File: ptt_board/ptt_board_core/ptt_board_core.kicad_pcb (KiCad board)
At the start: 2 copper layers, 25 x 25 mm, 14 parts, among them P0.03 TestPoint, P0.07 TestPoint, P0.30 TestPoint, P26 Conn_01x01_Pin, U1 SKB369

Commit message: [WIP] Started net rev of ptt board and radio board
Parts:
- removed BT1: MY-1632-03-R, Project_components:BAT-SMD_MY-1632-03
- removed Batt+1, P.0.31, P0.03, P0.07, P0.30, Reset1: TestPoint, TestPoint:TestPoint_Pad_D1.0mm
- removed IO1, P26: Conn_01x01_Pin, Connector_PinHeader_2.54mm:PinHeader_1x01_P2.54mm_Vertical
- added Batt1: TestPoint, TestPoint:TestPoint_Pad_D1.0mm, F.Cu at (102.5, 110.8)
- added Batt2: Conn_01x01_Pin, Connector_Pin:Pin_D1.0mm_L10.0mm, F.Cu at (106.5, 109.5)
- added GND3: TestPoint, TestPoint:TestPoint_Pad_D1.0mm, F.Cu at (101.2, 110.8)
- added IO2: TestPoint, TestPoint:TestPoint_Pad_D1.0mm, F.Cu at (100.0, 110.8)
- added P0.26: TestPoint, TestPoint:TestPoint_Pad_D1.0mm, F.Cu at (97.4, 110.8)
- added P026: Conn_01x01_Pin, Connector_Pin:Pin_D1.0mm_L10.0mm, F.Cu at (88.8, 100.8)
- added R1: 470k, Resistor_SMD:R_0603_1608Metric_Pad0.98x0.95mm_HandSolder, F.Cu at (93.5, 105.9)
- added SW1: RKB2SJG250SMTRLFS, Project_components:Push button C2927788, F.Cu at (100.0, 100.0)
- C1, C2, U1: moved to B.Cu
- CLK1: value Conn_01x01_Pin -> TestPoint; footprint Connector_PinHeader_2.54mm:PinHeader_1x01_P2.54mm_Vertical -> TestPoint:TestPoint_Pad_D1.0mm
- Gnd1: footprint Connector_PinHeader_2.54mm:PinHeader_1x01_P2.54mm_Vertical -> Connector_Pin:Pin_D1.0mm_L10.0mm
- moved C1 20.3 mm to (110.5, 96.0), turned to 0 degrees
- moved C2 15.7 mm to (110.5, 98.0)
- moved CLK1 11.3 mm to (98.7, 110.8), turned to -90 degrees
- moved Gnd1 4.51 mm to (111.5, 100.8)
- moved U1 0.51 mm to (100.0, 98.2), turned to 180 degrees
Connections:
- U1 pad 12: Net-(U1-P0.03) -> unconnected-(U1-P0.03-Pad12)
- U1 pad 14: Net-(U1-P0.07) -> unconnected-(U1-P0.07-Pad14)
- U1 pad 22: Reset -> unconnected-(U1-P0.21/~{RESET}-Pad22)
- U1 pad 4: Net-(P26-Pin_1) -> P0.26
- U1 pad 6: unconnected-(U1-P0.28-Pad6) -> P0.28
- U1 pad 8: Net-(U1-P0.30) -> unconnected-(U1-P0.30-Pad8)
- U1 pad 9: Net-(U1-P0.31) -> unconnected-(U1-P0.31-Pad9)
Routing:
- net GND: track 51.4 -> 2.31 mm, vias 2 -> 0
- net P0.26: track 0.00 -> 27.2 mm, vias 0 -> 2
- net Net-(P26-Pin_1): track 24.2 -> 0.00 mm, vias 1 -> 0
- net unconnected-(BT1-Pad1): track 21.1 -> 0.00 mm, vias 2 -> 0
- net Reset: track 9.42 -> 0.00 mm, vias 1 -> 0
- net Net-(U1-P0.31): track 8.42 -> 0.00 mm, vias 1 -> 0
- net Net-(U1-P0.07): track 8.40 -> 0.00 mm, vias 1 -> 0
- net Net-(U1-P0.30): track 8.28 -> 0.00 mm, vias 1 -> 0
- net Net-(U1-P0.03): track 8.15 -> 0.00 mm, vias 1 -> 0
- net +BATT: track 29.0 -> 21.9 mm, vias 1 -> 0
- net SWDIO: track 17.4 -> 20.7 mm
- net SWDCLK: track 20.6 -> 19.3 mm
- added copper zone on B.Cu, net GND
- added copper zone on F.Cu, net GND
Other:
- board size 25 x 25 mm -> 26.4 x 26.4 mm

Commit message: [WIP]
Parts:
- removed P0.26: TestPoint, TestPoint:TestPoint_Pad_D1.0mm
- removed P026: Conn_01x01_Pin, Connector_Pin:Pin_D1.0mm_L10.0mm
- added P019: Conn_01x01_Pin, Connector_Pin:Pin_D1.0mm_L10.0mm, F.Cu at (88.8, 100.8)
- moved IO2 3.01 mm to (98.2, 108.3)
- moved R1 2.69 mm to (92.5, 103.4)
- moved CLK1 2.57 mm to (99.5, 108.3)
- moved GND3 2.50 mm to (100.8, 108.3)
- moved Batt1 2.50 mm to (102.0, 108.3)
- moved U1 0.80 mm to (100.0, 99.0)
- moved C1 0.25 mm to (110.5, 96.2)
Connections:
- R1 pad 1: P0.26 -> P0.19
- SW1 pad 2: P0.26 -> P0.19
- U1 pad 21: unconnected-(U1-P0.19-Pad21) -> P0.19
- U1 pad 4: P0.26 -> unconnected-(U1-P0.26-Pad4)
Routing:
- net P0.26: track 27.2 -> 0.00 mm, vias 2 -> 0
- net P0.19: track 0.00 -> 15.0 mm, vias 0 -> 1
- net +BATT: track 21.9 -> 29.9 mm, vias 0 -> 1
- net SWDCLK: track 19.3 -> 21.6 mm
- net SWDIO: track 20.7 -> 22.3 mm
- net GND: track 2.31 -> 1.31 mm, vias 0 -> 13
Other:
- board size 26.4 x 26.4 mm -> 26.4 x 27.8 mm

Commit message: [WIP]
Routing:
- net GND: vias 13 -> 12
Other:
- board size 26.4 x 27.8 mm -> 26.4 x 26.4 mm
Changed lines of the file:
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@@
 		)
-	)
-	(gr_rect
-		(start 98 110)
-		(end 102 113.9)
-		(stroke
-			(width 0.2)
-			(type solid)
-		)
-		(fill no)
-		(layer "Edge.Cuts")
-	)
-	(gr_rect
-		(start 98.1 86.1)
-		(end 102.1 90)
-		(stroke
-			(width 0.2)
-			(type solid)
-		)
-		(fill no)
-		(layer "Edge.Cuts")
 	)
 	(gr_circle
@@
 	)
 	(via
-		(at 89.5 94.5)
+		(at 89.25 95.25)
 		(size 0.6)
 		(drill 0.3)
@@
 	(via
 		(at 96.1 111.2)
-		(size 0.6)
-		(drill 0.3)
-		(layers "F.Cu" "B.Cu")
-		(free yes)
-		(net 2)
-	)
-	(via
-		(at 109.5 94.5)
 		(size 0.6)
 		(drill 0.3)
@@
 		(polygon
 			(pts
-				(xy 114.5 94) (xy 85.5 94) (xy 85.5 114.5) (xy 114.5 114.25)
+				(xy 114.5 94.75) (xy 85.5 94.75) (xy 85.5 114.5) (xy 114.5 114.25)
 			)
 		)

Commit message: [WIP]
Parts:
- Batt2, Gnd1, P019: footprint Connector_Pin:Pin_D1.0mm_L10.0mm -> Connector_PinHeader_2.54mm:PinHeader_1x01_P2.54mm_Vertical
- moved Gnd1 22.9 mm to (89.2, 95.2)
- moved P019 3.29 mm to (89.2, 104.0)
- moved C2 2.64 mm to (109.2, 95.7), turned to -90 degrees
- moved U1 0.94 mm to (99.7, 98.1)
- moved C1 0.71 mm to (111.0, 95.7), turned to 90 degrees
- moved Batt2 0.25 mm to (106.5, 109.8)
- moved Batt1 0.12 mm to (101.9, 108.3)
- moved CLK1 0.12 mm to (99.4, 108.3)
- moved GND3 0.12 mm to (100.6, 108.3)
- moved IO2 0.12 mm to (98.1, 108.3)
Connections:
- U1 pad 6: P0.28 -> unconnected-(U1-P0.28-Pad6)
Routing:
- net GND: track 1.31 -> 6.17 mm, vias 12 -> 11
- net P0.19: track 15.0 -> 14.1 mm
- net SWDIO: track 22.3 -> 23.1 mm
- net SWDCLK: track 21.6 -> 22.2 mm
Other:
- board size 26.4 x 26.4 mm -> 26.1 x 26.4 mm

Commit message: [WIP]
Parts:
- C1, C2: footprint Project_components:C0603 -> Capacitor_SMD:C_0402_1005Metric_Pad0.74x0.62mm_HandSolder
- moved C2 0.54 mm to (109.5, 96.2)
- moved C1 0.48 mm to (111.0, 96.2)
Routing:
- net GND: track 6.17 -> 1.29 mm, vias 11 -> 16
- net P0.19: track 14.1 -> 14.8 mm

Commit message: [Housekeeping] Renamed project library
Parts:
- SW1: footprint Project_components:Push button C2927788 -> PTT_Project_library:Push button C2927788
- U1: footprint Project_components:SKYLAB_SKB369 -> PTT_Project_library:SKYLAB_SKB369
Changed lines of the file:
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@@
 		(embedded_fonts no)
 	)
-	(footprint "Project_components:Push button C2927788"
+	(footprint "PTT_Project_library:Push button C2927788"
 		(layer "F.Cu")
 		(at 100 100 180)
@@
 		)
 		(embedded_fonts no)
-		(model "/home/rbaruffa/Perso/OmniPTT/hardware/libraries/Project_components.3dshapes/SW-SMD_4P-L4.2-W3.2-P2.15-LS4.6.wrl"
+		(model "/home/rbaruffa/Perso/OmniPTT/hardware/libraries/PTT_Project_library.3dshapes/SW-SMD_4P-L4.2-W3.2-P2.15-LS4.6.wrl"
 			(offset
 				(xyz 0 -0 -0)
@@
 		)
 	)
-	(footprint "Project_components:SKYLAB_SKB369"
+	(footprint "PTT_Project_library:SKYLAB_SKB369"
 		(layer "B.Cu")
 		(at 99.65 98.13 180)
@@
 		)
 		(embedded_fonts no)
-		(model "${KIPRJMOD}/../../libraries/Project_components.3dshapes/SKB369.step"
+		(model "${KIPRJMOD}/../../libraries/PTT_Project_library.3dshapes/SKB369.step"
 			(offset
 				(xyz 0 0 0)

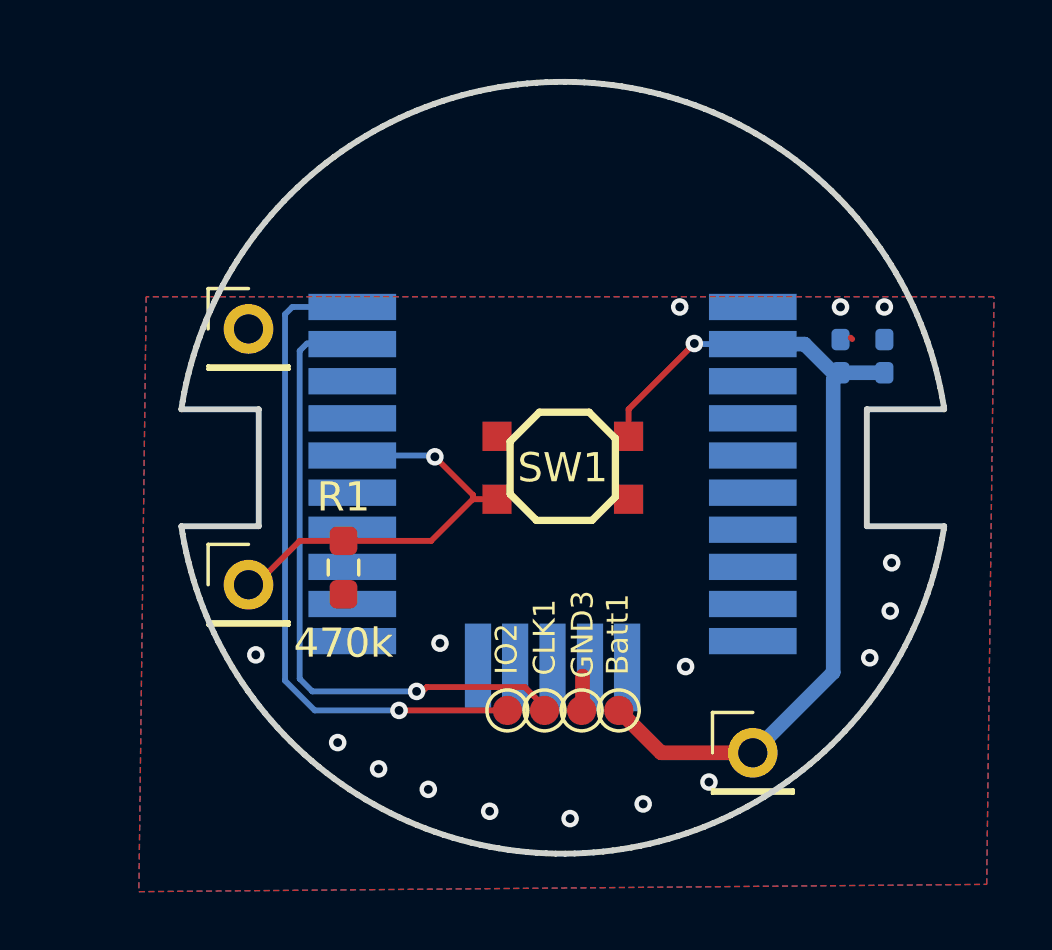
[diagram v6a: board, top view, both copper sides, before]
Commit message: [Feature] Cleaned up PCB and schematics. Add logo, checked schematic, layout and wiring
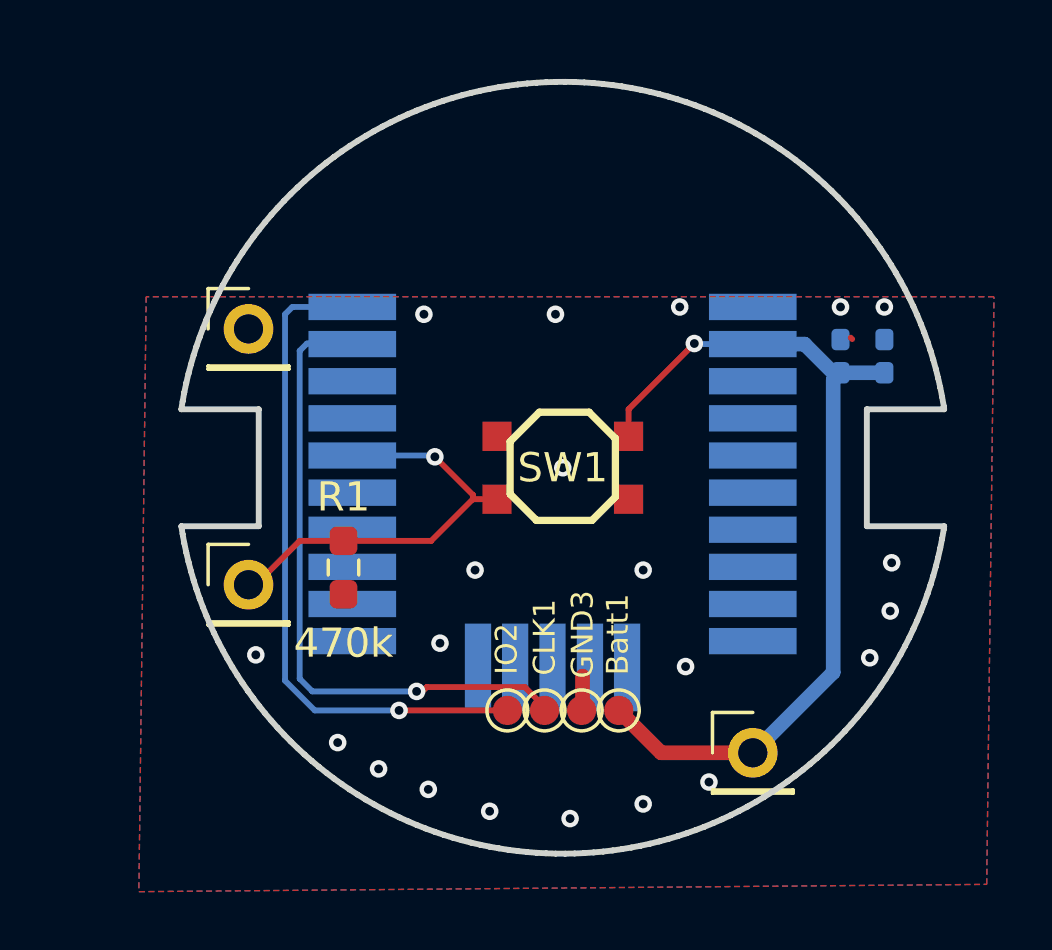
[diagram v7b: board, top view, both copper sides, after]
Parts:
- C1: value 0.1 uF -> 100nF
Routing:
- net GND: vias 16 -> 21
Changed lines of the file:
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@@
 		)
 		(embedded_fonts no)
-		(model "/home/rbaruffa/Perso/OmniPTT/hardware/libraries/PTT_Project_library.3dshapes/SW-SMD_4P-L4.2-W3.2-P2.15-LS4.6.wrl"
+		(model "${KIPRJMOD}/../../libraries/PTT_Project_library.3dshapes/SW-SMD_4P-L4.2-W3.2-P2.15-LS4.6.wrl"
 			(offset
 				(xyz 0 -0 -0)
@@
 			)
 		)
-		(property "Value" "0.1 uF"
+		(property "Value" "100nF"
 			(at 0.2 6 180)
 			(layer "B.Fab")
@@
 	)
 	(via
+		(at 95.25 94.75)
+		(size 0.6)
+		(drill 0.3)
+		(layers "F.Cu" "B.Cu")
+		(free yes)
+		(net 2)
+	)
+	(via
 		(at 109.5 94.5)
+		(size 0.6)
+		(drill 0.3)
+		(layers "F.Cu" "B.Cu")
+		(free yes)
+		(net 2)
+	)
+	(via
+		(at 100 100)
 		(size 0.6)
 		(drill 0.3)
@@
 	)
 	(via
+		(at 97 103.5)
+		(size 0.6)
+		(drill 0.3)
+		(layers "F.Cu" "B.Cu")
+		(free yes)
+		(net 2)
+	)
+	(via
 		(at 95.4 111)
 		(size 0.6)
@@
 	)
 	(via
+		(at 102.75 103.5)
+		(size 0.6)
+		(drill 0.3)
+		(layers "F.Cu" "B.Cu")
+		(free yes)
+		(net 2)
+	)
+	(via
 		(at 111.2 104.9)
 		(size 0.6)
@@
 		(size 0.6)
 		(drill 0.3)
+		(layers "F.Cu" "B.Cu")
+		(free yes)
+		(net 2)
+	)
+	(via
+		(at 99.75 94.75)
+		(size 0.6)
+		(drill 0.3)

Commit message: [Milestone] Last commit before pourchasing v2
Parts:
- added G***: LOGO, PTT_logo:omniPTT_logo, F.Cu at (100.4, 91.1)
- Batt2, Gnd1, P019: moved to B.Cu
- C1, C2: footprint Capacitor_SMD:C_0402_1005Metric_Pad0.74x0.62mm_HandSolder -> Capacitor_SMD:C_0603_1608Metric_Pad1.08x0.95mm_HandSolder
- moved C1 1.87 mm to (109.2, 95.7)
- moved C2 1.40 mm to (110.8, 95.7)
- turned Batt2 to 180 degrees
- turned Gnd1 to 180 degrees
- turned P019 to 180 degrees
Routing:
- net GND: track 1.29 -> 6.50 mm, vias 21 -> 22
- net +BATT: track 30.4 -> 29.9 mm
